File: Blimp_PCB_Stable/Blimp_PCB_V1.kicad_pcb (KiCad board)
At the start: 2 copper layers, 109.9 x 62 mm, 24 parts, among them J1 S8B-PH-K-S, J2 S4B-XH-A

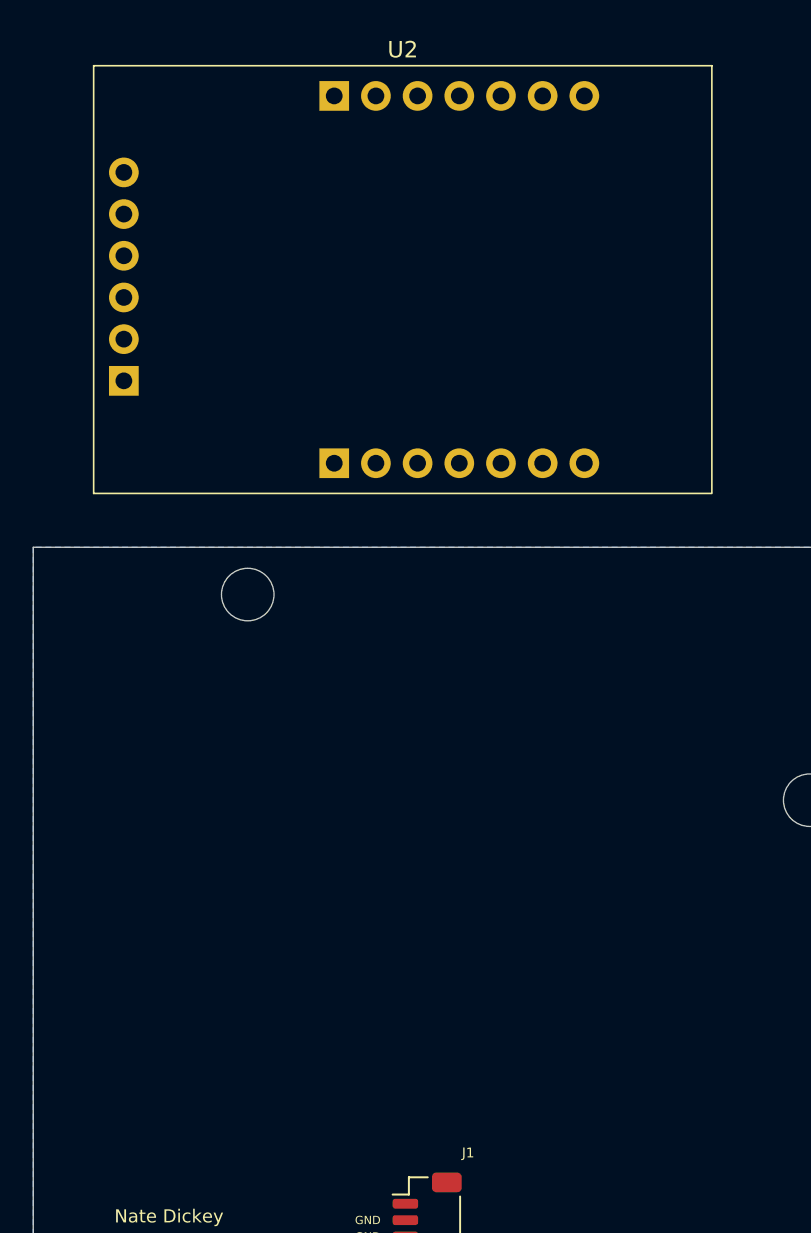
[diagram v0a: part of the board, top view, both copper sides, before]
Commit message: added Berry IMU 3D model
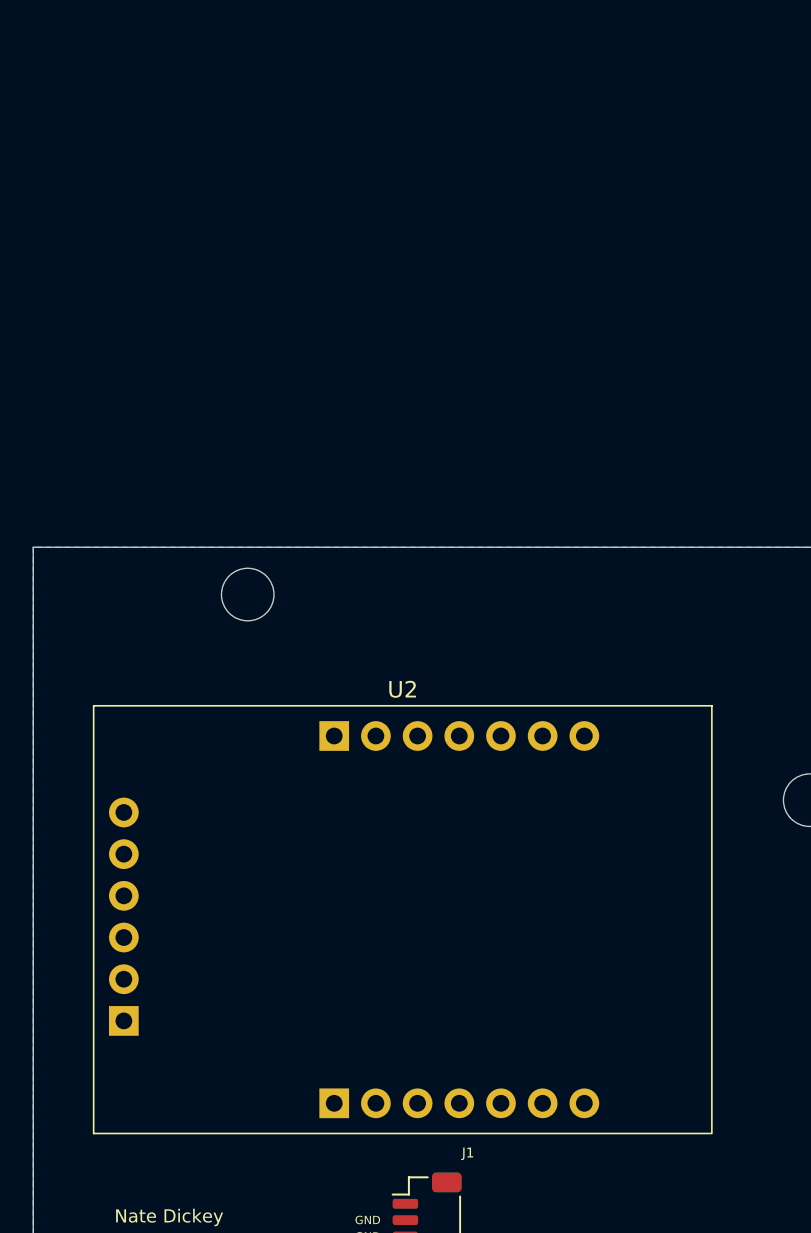
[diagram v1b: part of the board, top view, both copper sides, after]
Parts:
- R1: value 30K -> 30KΩ
- R2: value 7.5K -> 7.5KΩ
- moved U2 39.0 mm to (125.0, 91.7)
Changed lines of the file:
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@@
 			)
 		)
-		(property "Value" "7.5K"
+		(property "Value" "7.5KΩ"
 			(at 0 -1.2 0)
 			(layer "F.Fab")
@@
 	(footprint "Berry_IMU:Berry_IMU"
 		(layer "F.Cu")
-		(at 125.0159 52.6902)
+		(at 125.0159 91.6902)
 		(property "Reference" "U2"
 			(at 0 -14 0)
@@
 		)
 		(embedded_fonts no)
+		(model "${KIPRJMOD}/Stable Library/Berry_IMU/BerryIMUv3.8.step"
+			(offset
+				(xyz -1.6 3 1.5)
+			)
+			(scale
+				(xyz 1 1 1)
+			)
+			(rotate
+				(xyz -0 -0 -90)
+			)
+		)
 	)
 	(footprint "Buzz_Burn:Sahaj"
@@
 			)
 		)
-		(property "Value" "30K"
+		(property "Value" "30KΩ"
 			(at 0 1.25 0)
 			(layer "F.Fab")
